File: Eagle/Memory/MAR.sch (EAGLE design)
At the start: 38 parts

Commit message: added parts needed to finish boards
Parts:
- added DIP_8-11: 1825360-3, SamacSys_Parts:1825360-3
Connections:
- removed net N$11: BUS/PRGM_8-11.2B
- removed net N$12: BUS/PRGM_8-11.1B
- removed net N$13: BUS/PRGM_8-11.4B
- removed net N$14: BUS/PRGM_8-11.3B
- new net DP10: BUS/PRGM_8-11.3B, DIP_8-11.7
- new net DP11: BUS/PRGM_8-11.4B, DIP_8-11.8
- new net DP8: BUS/PRGM_8-11.1B, DIP_8-11.5
- new net DP9: BUS/PRGM_8-11.2B, DIP_8-11.6
- net VCC: now also DIP_8-11.1, DIP_8-11.2, DIP_8-11.3, DIP_8-11.4
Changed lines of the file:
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@@
 <part name="R11" library="rcl" library_urn="urn:adsk.eagle:library:334" deviceset="R-US_" device="0204/7" package3d_urn="urn:adsk.eagle:package:23498/2" value="220"/>
 <part name="R0" library="rcl" library_urn="urn:adsk.eagle:library:334" deviceset="R-US_" device="0204/7" package3d_urn="urn:adsk.eagle:package:23498/2" value="220"/>
+<part name="DIP_8-11" library="SamacSys_Parts" deviceset="1825360-3" device=""/>
 </parts>
 <sheets>
@@
 </instance>
 <instance part="DIP_0-7" gate="G$1" x="99.06" y="-99.06" smashed="yes" rot="R90">
-<attribute name="NAME" x="91.44" y="-80.01" size="1.778" layer="95" rot="R90" align="center-left"/>
-<attribute name="VALUE" x="93.98" y="-80.01" size="1.778" layer="96" rot="R90" align="center-left"/>
+<attribute name="NAME" x="121.92" y="-90.17" size="1.778" layer="95" rot="R90" align="center-left"/>
+<attribute name="VALUE" x="129.54" y="-87.63" size="1.778" layer="96" rot="R90" align="center-left"/>
 </instance>
 <instance part="PRGM_SWITCH" gate="G$1" x="182.88" y="-55.88" smashed="yes">
@@
 <attribute name="NAME" x="118.3386" y="-138.43" size="1.778" layer="95" rot="R270"/>
 <attribute name="VALUE" x="113.538" y="-138.43" size="1.778" layer="96" rot="R270"/>
+</instance>
+<instance part="DIP_8-11" gate="G$1" x="86.36" y="-96.52" smashed="yes" rot="R90">
+<attribute name="NAME" x="76.2" y="-85.09" size="1.778" layer="95" rot="R90" align="center-left"/>
+<attribute name="VALUE" x="78.74" y="-87.63" size="1.778" layer="96" rot="R90" align="center-left"/>
 </instance>
 </instances>
@@
 <wire x1="101.6" y1="-99.06" x2="101.6" y2="-101.6" width="0.1524" layer="91"/>
 <junction x="101.6" y="-101.6"/>
-<wire x1="99.06" y1="-101.6" x2="96.52" y2="-101.6" width="0.1524" layer="91"/>
+<pinref part="DIP_8-11" gate="G$1" pin="1"/>
+<wire x1="86.36" y1="-96.52" x2="86.36" y2="-101.6" width="0.1524" layer="91"/>
+<wire x1="86.36" y1="-101.6" x2="88.9" y2="-101.6" width="0.1524" layer="91"/>
 <junction x="99.06" y="-101.6"/>
-<label x="96.52" y="-101.6" size="1.778" layer="95" rot="R180"/>
+<wire x1="88.9" y1="-101.6" x2="91.44" y2="-101.6" width="0.1524" layer="91"/>
+<wire x1="91.44" y1="-101.6" x2="93.98" y2="-101.6" width="0.1524" layer="91"/>
+<wire x1="93.98" y1="-101.6" x2="99.06" y2="-101.6" width="0.1524" layer="91"/>
+<wire x1="99.06" y1="-101.6" x2="99.06" y2="-104.14" width="0.1524" layer="91"/>
+<pinref part="DIP_8-11" gate="G$1" pin="4"/>
+<wire x1="93.98" y1="-96.52" x2="93.98" y2="-101.6" width="0.1524" layer="91"/>
+<junction x="93.98" y="-101.6"/>
+<pinref part="DIP_8-11" gate="G$1" pin="3"/>
+<wire x1="91.44" y1="-96.52" x2="91.44" y2="-101.6" width="0.1524" layer="91"/>
+<junction x="91.44" y="-101.6"/>
+<pinref part="DIP_8-11" gate="G$1" pin="2"/>
+<wire x1="88.9" y1="-96.52" x2="88.9" y2="-101.6" width="0.1524" layer="91"/>
+<junction x="88.9" y="-101.6"/>
+<label x="99.06" y="-104.14" size="1.778" layer="95" rot="R270"/>
 </segment>
 <segment>
@@
 </segment>
 </net>
-<net name="N$11" class="0">
+<net name="DP9" class="0">
 <segment>
 <pinref part="BUS/PRGM_8-11" gate="G$1" pin="2B"/>
@@
 <label x="66.04" y="25.4" size="1.778" layer="95" rot="R180"/>
 </segment>
-</net>
-<net name="N$12" class="0">
+<segment>
+<pinref part="DIP_8-11" gate="G$1" pin="6"/>
+<wire x1="91.44" y1="-76.2" x2="91.44" y2="-73.66" width="0.1524" layer="91"/>
+<label x="91.44" y="-73.66" size="1.778" layer="95" rot="R90"/>
+</segment>
+</net>
+<net name="DP8" class="0">
 <segment>
 <pinref part="BUS/PRGM_8-11" gate="G$1" pin="1B"/>
@@
 <label x="66.04" y="33.02" size="1.778" layer="95" rot="R180"/>
 </segment>
-</net>
-<net name="N$13" class="0">
+<segment>
+<pinref part="DIP_8-11" gate="G$1" pin="5"/>
+<wire x1="93.98" y1="-76.2" x2="93.98" y2="-73.66" width="0.1524" layer="91"/>
+<label x="93.98" y="-73.66" size="1.778" layer="95" rot="R90"/>
+</segment>
+</net>
+<net name="DP11" class="0">
 <segment>
 <pinref part="BUS/PRGM_8-11" gate="G$1" pin="4B"/>
@@
 <label x="99.06" y="30.48" size="1.778" layer="95"/>
 </segment>
-</net>
-<net name="N$14" class="0">
+<segment>
+<pinref part="DIP_8-11" gate="G$1" pin="8"/>
+<wire x1="86.36" y1="-76.2" x2="86.36" y2="-73.66" width="0.1524" layer="91"/>
+<label x="86.36" y="-73.66" size="1.778" layer="95" rot="R90"/>
+</segment>
+</net>
+<net name="DP10" class="0">
 <segment>
 <pinref part="BUS/PRGM_8-11" gate="G$1" pin="3B"/>
@@
 <label x="99.06" y="22.86" size="1.778" layer="95"/>
 </segment>
-</net>
+<segment>
+<pinref part="DIP_8-11" gate="G$1" pin="7"/>
+<wire x1="88.9" y1="-76.2" x2="88.9" y2="-73.66" width="0.1524" layer="91"/>
+<label x="88.9" y="-73.66" size="1.778" layer="95" rot="R90"/>
+</segment>
+</net>

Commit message: Finished IR
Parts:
- removed BUS: 55959-1630, SamacSys_Parts:55959-1630
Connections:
- net B0: no longer BUS.1
- net B1: no longer BUS.3
- net B10: no longer BUS.6
- net B11: no longer BUS.8
- net B2: no longer BUS.5
- net B3: no longer BUS.7
- net B4: no longer BUS.9
- net B5: no longer BUS.11
- net B6: no longer BUS.13
- net B7: no longer BUS.15
- net B8: no longer BUS.2
- net B9: no longer BUS.4
- net CLK: no longer BUS.14
- net GND: no longer BUS.16
- net MARI: no longer BUS.10
- net VCC: no longer BUS.12
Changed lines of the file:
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@@
 <part name="MAR_8-11" library="SamacSys_Parts" deviceset="SN74BCT374N" device=""/>
 <part name="MAR_0-7" library="SamacSys_Parts" deviceset="SN74BCT374N" device=""/>
-<part name="BUS" library="SamacSys_Parts" deviceset="55959-1630" device=""/>
 <part name="BUS/PRGM_8-11" library="SamacSys_Parts" deviceset="SN74HC157N" device=""/>
 <part name="BUS/PRGM_4-7" library="SamacSys_Parts" deviceset="SN74HC157N" device=""/>
@@
 <attribute name="VALUE" x="143.51" y="2.54" size="1.778" layer="96" align="center-left"/>
 </instance>
-<instance part="BUS" gate="G$1" x="193.04" y="35.56" smashed="yes">
-<attribute name="NAME" x="212.09" y="43.18" size="1.778" layer="95" align="center-left"/>
-<attribute name="VALUE" x="212.09" y="40.64" size="1.778" layer="96" align="center-left"/>
-</instance>
 <instance part="BUS/PRGM_8-11" gate="G$1" x="68.58" y="38.1" smashed="yes">
 <attribute name="NAME" x="92.71" y="45.72" size="1.778" layer="95" align="center-left"/>
@@
 <net name="B0" class="0">
 <segment>
-<pinref part="BUS" gate="G$1" pin="1"/>
 <wire x1="193.04" y1="35.56" x2="190.5" y2="35.56" width="0.1524" layer="91"/>
 <label x="190.5" y="35.56" size="1.778" layer="95" rot="R180"/>
@@
 <net name="B1" class="0">
 <segment>
-<pinref part="BUS" gate="G$1" pin="3"/>
 <wire x1="193.04" y1="33.02" x2="190.5" y2="33.02" width="0.1524" layer="91"/>
 <label x="190.5" y="33.02" size="1.778" layer="95" rot="R180"/>
@@
 <net name="B2" class="0">
 <segment>
-<pinref part="BUS" gate="G$1" pin="5"/>
 <wire x1="193.04" y1="30.48" x2="190.5" y2="30.48" width="0.1524" layer="91"/>
 <label x="190.5" y="30.48" size="1.778" layer="95" rot="R180"/>
@@
 <net name="B3" class="0">
 <segment>
-<pinref part="BUS" gate="G$1" pin="7"/>
 <wire x1="193.04" y1="27.94" x2="190.5" y2="27.94" width="0.1524" layer="91"/>
 <label x="190.5" y="27.94" size="1.778" layer="95" rot="R180"/>
@@
 <net name="B4" class="0">
 <segment>
-<pinref part="BUS" gate="G$1" pin="9"/>
 <wire x1="193.04" y1="25.4" x2="190.5" y2="25.4" width="0.1524" layer="91"/>
 <label x="190.5" y="25.4" size="1.778" layer="95" rot="R180"/>
@@
 <net name="B5" class="0">
 <segment>
-<pinref part="BUS" gate="G$1" pin="11"/>
 <wire x1="193.04" y1="22.86" x2="190.5" y2="22.86" width="0.1524" layer="91"/>
 <label x="190.5" y="22.86" size="1.778" layer="95" rot="R180"/>
@@
 </segment>
 <segment>
-<pinref part="BUS" gate="G$1" pin="13"/>
 <wire x1="193.04" y1="20.32" x2="190.5" y2="20.32" width="0.1524" layer="91"/>
 <label x="190.5" y="20.32" size="1.778" layer="95" rot="R180"/>
@@
 </segment>
 <segment>
-<pinref part="BUS" gate="G$1" pin="15"/>
 <wire x1="193.04" y1="17.78" x2="190.5" y2="17.78" width="0.1524" layer="91"/>
 <label x="190.5" y="17.78" size="1.778" layer="95" rot="R180"/>
@@
 </segment>
 <segment>
-<pinref part="BUS" gate="G$1" pin="2"/>
 <wire x1="215.9" y1="35.56" x2="218.44" y2="35.56" width="0.1524" layer="91"/>
 <label x="218.44" y="35.56" size="1.778" layer="95"/>
@@
 </segment>
 <segment>
-<pinref part="BUS" gate="G$1" pin="4"/>
 <wire x1="215.9" y1="33.02" x2="218.44" y2="33.02" width="0.1524" layer="91"/>
 <label x="218.44" y="33.02" size="1.778" layer="95"/>
@@
 </segment>
 <segment>
-<pinref part="BUS" gate="G$1" pin="6"/>
 <wire x1="215.9" y1="30.48" x2="218.44" y2="30.48" width="0.1524" layer="91"/>
 <label x="218.44" y="30.48" size="1.778" layer="95"/>
@@
 </segment>
 <segment>
-<pinref part="BUS" gate="G$1" pin="8"/>
 <wire x1="215.9" y1="27.94" x2="218.44" y2="27.94" width="0.1524" layer="91"/>
 <label x="218.44" y="27.94" size="1.778" layer="95"/>
@@
 <net name="CLK" class="0">
 <segment>
-<pinref part="BUS" gate="G$1" pin="14"/>
 <wire x1="215.9" y1="20.32" x2="218.44" y2="20.32" width="0.1524" layer="91"/>
 <label x="218.44" y="20.32" size="1.778" layer="95"/>
@@
 </segment>
 <segment>
-<pinref part="BUS" gate="G$1" pin="10"/>
 <wire x1="215.9" y1="25.4" x2="218.44" y2="25.4" width="0.1524" layer="91"/>
 <label x="218.44" y="25.4" size="1.778" layer="95"/>
@@
 </segment>
 <segment>
-<pinref part="BUS" gate="G$1" pin="12"/>
 <wire x1="215.9" y1="22.86" x2="218.44" y2="22.86" width="0.1524" layer="91"/>
 <label x="218.44" y="22.86" size="1.778" layer="95"/>
@@
 <net name="GND" class="0">
 <segment>
-<pinref part="BUS" gate="G$1" pin="16"/>
 <wire x1="215.9" y1="17.78" x2="218.44" y2="17.78" width="0.1524" layer="91"/>
 <label x="218.44" y="17.78" size="1.778" layer="95"/>

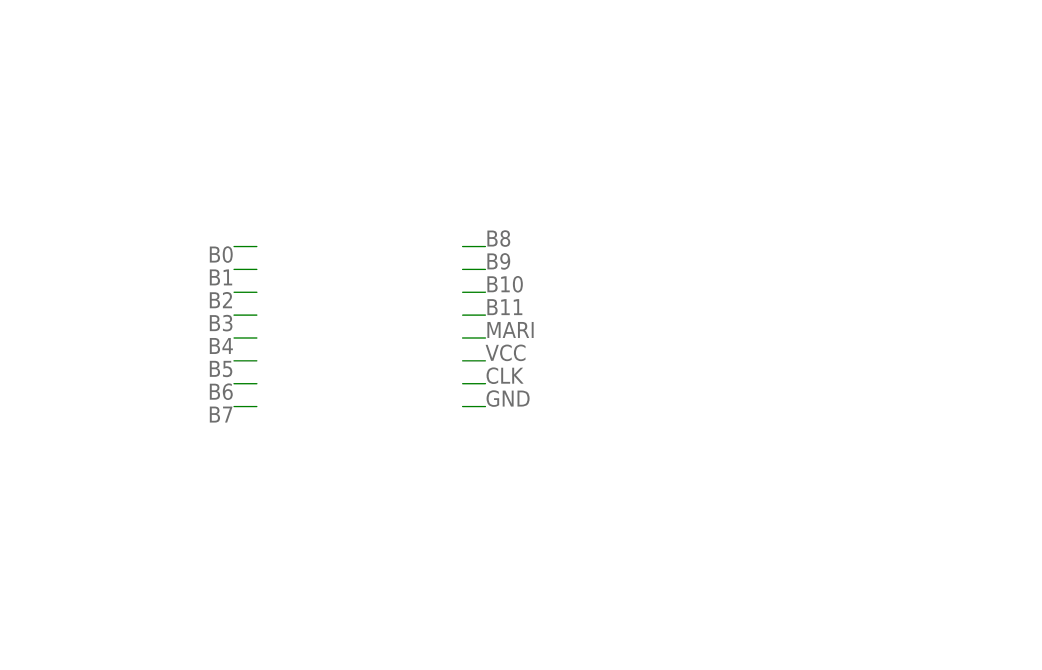
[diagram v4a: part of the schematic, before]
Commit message: added HLT to MAR for prgm mode
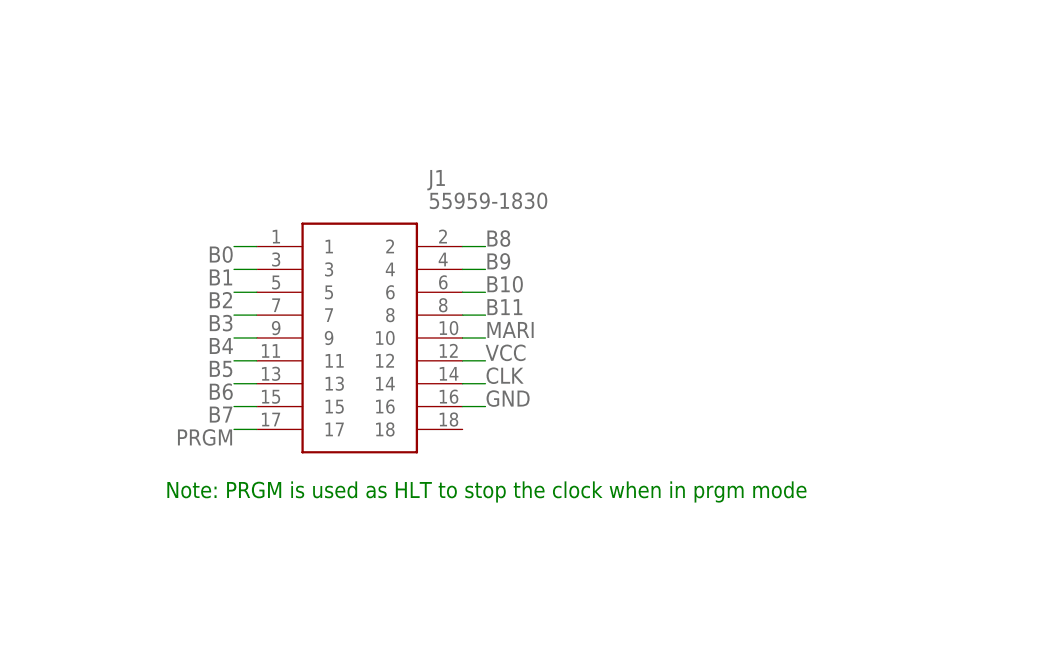
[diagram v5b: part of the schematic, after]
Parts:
- added J1: 55959-1830, SamacSys_Parts:55959-1830
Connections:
- net B0: now also J1.1
- net B1: now also J1.3
- net B10: now also J1.6
- net B11: now also J1.8
- net B2: now also J1.5
- net B3: now also J1.7
- net B4: now also J1.9
- net B5: now also J1.11
- net B6: now also J1.13
- net B7: now also J1.15
- net B8: now also J1.2
- net B9: now also J1.4
- net CLK: now also J1.14
- net GND: now also J1.16
- net MARI: now also J1.10
- net PRGM: now also J1.17
- net VCC: now also J1.12
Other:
- note added: "Note: PRGM is used as HLT to stop the clock when in prgm mode"
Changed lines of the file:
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@@
 <part name="R0" library="rcl" library_urn="urn:adsk.eagle:library:334" deviceset="R-US_" device="0204/7" package3d_urn="urn:adsk.eagle:package:23498/2" value="220"/>
 <part name="DIP_8-11" library="SamacSys_Parts" deviceset="1825360-3" device=""/>
+<part name="J1" library="SamacSys_Parts" deviceset="55959-1830" device=""/>
 </parts>
 <sheets>
 <sheet>
 <plain>
+<text x="182.88" y="7.62" size="1.778" layer="91">Note: PRGM is used as HLT to stop the clock when in prgm mode</text>
 </plain>
 <instances>
@@
 <attribute name="VALUE" x="78.74" y="-87.63" size="1.778" layer="96" rot="R90" align="center-left"/>
 </instance>
+<instance part="J1" gate="G$1" x="193.04" y="35.56" smashed="yes">
+<attribute name="NAME" x="212.09" y="43.18" size="1.778" layer="95" align="center-left"/>
+<attribute name="VALUE" x="212.09" y="40.64" size="1.778" layer="96" align="center-left"/>
+</instance>
 </instances>
 <busses>
@@
 <label x="180.34" y="-58.42" size="1.778" layer="95" rot="R180"/>
 </segment>
+<segment>
+<pinref part="J1" gate="G$1" pin="17"/>
+<wire x1="193.04" y1="15.24" x2="190.5" y2="15.24" width="0.1524" layer="91"/>
+<label x="190.5" y="15.24" size="1.778" layer="95" rot="R180"/>
+</segment>
 </net>
 <net name="ARD0" class="0">
@@
 <wire x1="193.04" y1="35.56" x2="190.5" y2="35.56" width="0.1524" layer="91"/>
 <label x="190.5" y="35.56" size="1.778" layer="95" rot="R180"/>
+<pinref part="J1" gate="G$1" pin="1"/>
 </segment>
 <segment>
@@
 <wire x1="193.04" y1="33.02" x2="190.5" y2="33.02" width="0.1524" layer="91"/>
 <label x="190.5" y="33.02" size="1.778" layer="95" rot="R180"/>
+<pinref part="J1" gate="G$1" pin="3"/>
 </segment>
 <segment>
@@
 <wire x1="193.04" y1="30.48" x2="190.5" y2="30.48" width="0.1524" layer="91"/>
 <label x="190.5" y="30.48" size="1.778" layer="95" rot="R180"/>
+<pinref part="J1" gate="G$1" pin="5"/>
 </segment>
 <segment>
@@
 <wire x1="193.04" y1="27.94" x2="190.5" y2="27.94" width="0.1524" layer="91"/>
 <label x="190.5" y="27.94" size="1.778" layer="95" rot="R180"/>
+<pinref part="J1" gate="G$1" pin="7"/>
 </segment>
 <segment>
@@
 <wire x1="193.04" y1="25.4" x2="190.5" y2="25.4" width="0.1524" layer="91"/>
 <label x="190.5" y="25.4" size="1.778" layer="95" rot="R180"/>
+<pinref part="J1" gate="G$1" pin="9"/>
 </segment>
 <segment>
@@
 <wire x1="193.04" y1="22.86" x2="190.5" y2="22.86" width="0.1524" layer="91"/>
 <label x="190.5" y="22.86" size="1.778" layer="95" rot="R180"/>
+<pinref part="J1" gate="G$1" pin="11"/>
 </segment>
 <segment>
@@
 <wire x1="193.04" y1="20.32" x2="190.5" y2="20.32" width="0.1524" layer="91"/>
 <label x="190.5" y="20.32" size="1.778" layer="95" rot="R180"/>
+<pinref part="J1" gate="G$1" pin="13"/>
 </segment>
 </net>
@@
 <wire x1="193.04" y1="17.78" x2="190.5" y2="17.78" width="0.1524" layer="91"/>
 <label x="190.5" y="17.78" size="1.778" layer="95" rot="R180"/>
+<pinref part="J1" gate="G$1" pin="15"/>
 </segment>
 </net>
@@
 <wire x1="215.9" y1="35.56" x2="218.44" y2="35.56" width="0.1524" layer="91"/>
 <label x="218.44" y="35.56" size="1.778" layer="95"/>
+<pinref part="J1" gate="G$1" pin="2"/>
 </segment>
 </net>
@@
 <wire x1="215.9" y1="33.02" x2="218.44" y2="33.02" width="0.1524" layer="91"/>
 <label x="218.44" y="33.02" size="1.778" layer="95"/>
+<pinref part="J1" gate="G$1" pin="4"/>
 </segment>
 </net>
@@
 <wire x1="215.9" y1="30.48" x2="218.44" y2="30.48" width="0.1524" layer="91"/>
 <label x="218.44" y="30.48" size="1.778" layer="95"/>
+<pinref part="J1" gate="G$1" pin="6"/>
 </segment>
 </net>
@@
 <wire x1="215.9" y1="27.94" x2="218.44" y2="27.94" width="0.1524" layer="91"/>
 <label x="218.44" y="27.94" size="1.778" layer="95"/>
+<pinref part="J1" gate="G$1" pin="8"/>
 </segment>
 </net>
@@
 <wire x1="215.9" y1="20.32" x2="218.44" y2="20.32" width="0.1524" layer="91"/>
 <label x="218.44" y="20.32" size="1.778" layer="95"/>
+<pinref part="J1" gate="G$1" pin="14"/>
 </segment>
 <segment>
@@
 <wire x1="215.9" y1="25.4" x2="218.44" y2="25.4" width="0.1524" layer="91"/>
 <label x="218.44" y="25.4" size="1.778" layer="95"/>
+<pinref part="J1" gate="G$1" pin="10"/>
 </segment>
 </net>
@@
 <wire x1="215.9" y1="22.86" x2="218.44" y2="22.86" width="0.1524" layer="91"/>
 <label x="218.44" y="22.86" size="1.778" layer="95"/>
+<pinref part="J1" gate="G$1" pin="12"/>
 </segment>
 </net>
@@
 <wire x1="215.9" y1="17.78" x2="218.44" y2="17.78" width="0.1524" layer="91"/>
 <label x="218.44" y="17.78" size="1.778" layer="95"/>
-</segment>
-<segment>
+<pinref part="J1" gate="G$1" pin="16"/>
+</segment>
+<segment>

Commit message: finished most boards
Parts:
- added C1, C2, C3, C4: (no value), rcl:C-US025-024X044
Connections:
- net GND: now also C1.1, C2.1, C3.1, C4.1
- net VCC: now also C1.2, C2.2, C3.2, C4.2
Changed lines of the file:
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@@
 <part name="DIP_8-11" library="SamacSys_Parts" deviceset="1825360-3" device=""/>
 <part name="J1" library="SamacSys_Parts" deviceset="55959-1830" device=""/>
+<part name="C1" library="rcl" library_urn="urn:adsk.eagle:library:334" deviceset="C-US" device="025-024X044" package3d_urn="urn:adsk.eagle:package:23630/1"/>
+<part name="C2" library="rcl" library_urn="urn:adsk.eagle:library:334" deviceset="C-US" device="025-024X044" package3d_urn="urn:adsk.eagle:package:23630/1"/>
+<part name="C3" library="rcl" library_urn="urn:adsk.eagle:library:334" deviceset="C-US" device="025-024X044" package3d_urn="urn:adsk.eagle:package:23630/1"/>
+<part name="C4" library="rcl" library_urn="urn:adsk.eagle:library:334" deviceset="C-US" device="025-024X044" package3d_urn="urn:adsk.eagle:package:23630/1"/>
 </parts>
 <sheets>
@@
 <attribute name="NAME" x="212.09" y="43.18" size="1.778" layer="95" align="center-left"/>
 <attribute name="VALUE" x="212.09" y="40.64" size="1.778" layer="96" align="center-left"/>
+</instance>
+<instance part="C1" gate="G$1" x="198.12" y="-17.78" smashed="yes" rot="R180">
+<attribute name="NAME" x="197.104" y="-18.415" size="1.778" layer="95" rot="R180"/>
+<attribute name="VALUE" x="197.104" y="-13.589" size="1.778" layer="96" rot="R180"/>
+</instance>
+<instance part="C2" gate="G$1" x="213.36" y="-17.78" smashed="yes" rot="R180">
+<attribute name="NAME" x="212.344" y="-18.415" size="1.778" layer="95" rot="R180"/>
+<attribute name="VALUE" x="212.344" y="-13.589" size="1.778" layer="96" rot="R180"/>
+</instance>
+<instance part="C3" gate="G$1" x="228.6" y="-17.78" smashed="yes" rot="R180">
+<attribute name="NAME" x="227.584" y="-18.415" size="1.778" layer="95" rot="R180"/>
+<attribute name="VALUE" x="227.584" y="-13.589" size="1.778" layer="96" rot="R180"/>
+</instance>
+<instance part="C4" gate="G$1" x="243.84" y="-17.78" smashed="yes" rot="R180">
+<attribute name="NAME" x="242.824" y="-18.415" size="1.778" layer="95" rot="R180"/>
+<attribute name="VALUE" x="242.824" y="-13.589" size="1.778" layer="96" rot="R180"/>
 </instance>
 </instances>
@@
 <label x="218.44" y="22.86" size="1.778" layer="95"/>
 <pinref part="J1" gate="G$1" pin="12"/>
+</segment>
+<segment>
+<pinref part="C1" gate="G$1" pin="2"/>
+<wire x1="198.12" y1="-12.7" x2="198.12" y2="-5.08" width="0.1524" layer="91"/>
+<pinref part="C4" gate="G$1" pin="2"/>
+<wire x1="198.12" y1="-5.08" x2="213.36" y2="-5.08" width="0.1524" layer="91"/>
+<wire x1="213.36" y1="-5.08" x2="220.98" y2="-5.08" width="0.1524" layer="91"/>
+<wire x1="220.98" y1="-5.08" x2="228.6" y2="-5.08" width="0.1524" layer="91"/>
+<wire x1="228.6" y1="-5.08" x2="243.84" y2="-5.08" width="0.1524" layer="91"/>
+<wire x1="243.84" y1="-5.08" x2="243.84" y2="-12.7" width="0.1524" layer="91"/>
+<wire x1="220.98" y1="-5.08" x2="220.98" y2="-2.54" width="0.1524" layer="91"/>
+<junction x="220.98" y="-5.08"/>
+<label x="220.98" y="-2.54" size="1.778" layer="95" rot="R90"/>
+<pinref part="C2" gate="G$1" pin="2"/>
+<wire x1="213.36" y1="-5.08" x2="213.36" y2="-12.7" width="0.1524" layer="91"/>
+<junction x="213.36" y="-5.08"/>
+<pinref part="C3" gate="G$1" pin="2"/>
+<wire x1="228.6" y1="-12.7" x2="228.6" y2="-5.08" width="0.1524" layer="91"/>
+<junction x="228.6" y="-5.08"/>
 </segment>
 </net>
@@
 <label x="121.92" y="-160.02" size="1.778" layer="95"/>
 </segment>
-</net>
+<segment>
+<pinref part="C1" gate="G$1" pin="1"/>
+<wire x1="198.12" y1="-20.32" x2="198.12" y2="-30.48" width="0.1524" layer="91"/>
+<wire x1="198.12" y1="-30.48" x2="213.36" y2="-30.48" width="0.1524" layer="91"/>
+<pinref part="C4" gate="G$1" pin="1"/>
+<wire x1="213.36" y1="-30.48" x2="223.52" y2="-30.48" width="0.1524" layer="91"/>
+<wire x1="223.52" y1="-30.48" x2="228.6" y2="-30.48" width="0.1524" layer="91"/>
+<wire x1="228.6" y1="-30.48" x2="243.84" y2="-30.48" width="0.1524" layer="91"/>
+<wire x1="243.84" y1="-30.48" x2="243.84" y2="-20.32" width="0.1524" layer="91"/>
+<wire x1="223.52" y1="-30.48" x2="223.52" y2="-33.02" width="0.1524" layer="91"/>
+<junction x="223.52" y="-30.48"/>
+<label x="223.52" y="-33.02" size="1.778" layer="95" rot="R270"/>
+<pinref part="C2" gate="G$1" pin="1"/>
+<wire x1="213.36" y1="-20.32" x2="213.36" y2="-30.48" width="0.1524" layer="91"/>
+<junction x="213.36" y="-30.48"/>
+<pinref part="C3" gate="G$1" pin="1"/>
+<wire x1="228.6" y1="-30.48" x2="228.6" y2="-20.32" width="0.1524" layer="91"/>
+<junction x="228.6" y="-30.48"/>
+</segment>
+</net>
